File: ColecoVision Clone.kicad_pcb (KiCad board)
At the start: 2 copper layers, 149.4 x 99.1 mm, 141 parts, among them J1 Cartridge Slot, J2 Composite video, J3 PJ-102A, J4 RCJ-017, J5 Controller Port 1, J6 Controller Port 2, Q1 2n4401, Q2 Q_NJFET_DGS, Q3 2N3904, Q4 2N3904, Q5 2N3904, SW1 Power Toggle, SW2 Reset, U1 Z80CPU, U10 SN76489AN, U12 74LS138 (Mem. Mapped), U13 74LS138 (I/O), U14 74LS02, U15 Controller 1, U16 Controller 2, U17 74LS05, U18 74LS05, U19 74HC04, U2 Work RAM, U20 74LS74, U21 74HC04, U22 74LS74, U23 74HCT00, U24 TPS60403DBVR, U3 BIOS ROM 27C256, U4 74HCT04, U5 TMS9918A, U6 74LS574, U7 74LS574, U8 74LS574, U9 VRAM, X1 14.31818MHz

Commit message: TMS passive
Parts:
- moved C6 108.3 mm to (8.89, 85.7), turned to 90 degrees
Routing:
- net GND: track 841.0 -> 847.8 mm
- net VCC: track 776.2 -> 779.3 mm
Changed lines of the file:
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@@
     (thickness 1.6)
     (drawings 17)
-    (tracks 4420)
+    (tracks 4426)
     (zones 0)
     (modules 141)
@@
     (tags "resistor 0805")
     (attr smd)
-    (fp_text reference R7 (at 0 -1.7 90) (layer F.SilkS)
+    (fp_text reference R7 (at 3.6665 0.0635 90) (layer F.SilkS)
       (effects (font (size 1 1) (thickness 0.15)))
     )
@@
       (effects (font (size 1 1) (thickness 0.15)) (justify mirror))
     )
-    (fp_text value 2.7µH (at 0 -1.8 270) (layer Dwgs.User)
+    (fp_text value 2.7µH (at 0 -1.8 270) (layer Dwgs.User) hide
       (effects (font (size 1 1) (thickness 0.15)))
     )
@@
     (tags "capacitor 0805")
     (attr smd)
-    (fp_text reference C31 (at 0 -1.75) (layer F.SilkS)
+    (fp_text reference C31 (at -3.7465 0.8255) (layer F.SilkS)
       (effects (font (size 1 1) (thickness 0.15)))
     )
@@
       (effects (font (size 1 1) (thickness 0.15)))
     )
-    (fp_text user %R (at 0 -1.75) (layer F.Fab)
+    (fp_text user %R (at -3.81 0.8255) (layer F.Fab)
       (effects (font (size 1 1) (thickness 0.15)))
     )
@@
   )
   (module Capacitors_SMD:C_0805_HandSoldering (layer F.Cu)
-    (at 111.978 118.992)
+    (at 8.89 85.725 90)
     (descr "Capacitor SMD 0805, hand soldering")
     (tags "capacitor 0805")
     (attr smd)
-    (fp_text reference C6 (at 0 -1.75) (layer F.SilkS)
+    (fp_text reference C6 (at 0 -1.75 90) (layer F.SilkS)
       (effects (font (size 1 1) (thickness 0.15)))
     )
-    (fp_text value 0.1µF (at 0 1.75) (layer F.Fab)
+    (fp_text value 0.1µF (at 0 1.75 90) (layer F.Fab)
       (effects (font (size 1 1) (thickness 0.15)))
     )
-    (fp_text user %R (at 0 -1.75) (layer F.Fab)
+    (fp_text user %R (at 0 -1.75 90) (layer F.Fab)
       (effects (font (size 1 1) (thickness 0.15)))
     )
@@
     (fp_line (start 2.25 0.87) (end 2.25 -0.88) (layer F.CrtYd) (width 0.05))
     (fp_line (start 2.25 0.87) (end -2.25 0.87) (layer F.CrtYd) (width 0.05))
-    (pad 1 smd rect (at -1.25 0) (size 1.5 1.25) (layers F.Cu F.Paste F.Mask)
+    (pad 1 smd rect (at -1.25 0 90) (size 1.5 1.25) (layers F.Cu F.Paste F.Mask)
       (net 19 VCC))
-    (pad 2 smd rect (at 1.25 0) (size 1.5 1.25) (layers F.Cu F.Paste F.Mask)
+    (pad 2 smd rect (at 1.25 0 90) (size 1.5 1.25) (layers F.Cu F.Paste F.Mask)
       (net 10 GND))
     (model Capacitors_SMD.3dshapes/C_0805.wrl
@@
   (segment (start 11.002 35.386) (end 11.002 34.906) (width 0.25) (layer F.Cu) (net 10))
   (segment (start 13.208 37.592) (end 11.002 35.386) (width 0.25) (layer F.Cu) (net 10))
+  (segment (start 11.792 79.248) (end 12.192 79.248) (width 0.25) (layer F.Cu) (net 10))
+  (segment (start 8.89 82.15) (end 11.792 79.248) (width 0.25) (layer F.Cu) (net 10))
+  (segment (start 8.89 84.475) (end 8.89 82.15) (width 0.25) (layer F.Cu) (net 10))
   (segment (start 7.214 92.837) (end 7.7855 92.2655) (width 0.25) (layer F.Cu) (net 19) (status 10))
   (segment (start 6.764 92.837) (end 7.214 92.837) (width 0.25) (layer F.Cu) (net 19) (status 30))
@@
   (segment (start 19.972 38.862) (end 18.972 38.862) (width 0.25) (layer F.Cu) (net 19))
   (segment (start 18.972 38.862) (end 18.346999 38.236999) (width 0.25) (layer F.Cu) (net 19))
+  (segment (start 7.7855 89.0795) (end 7.7855 89.5735) (width 0.25) (layer F.Cu) (net 19))
+  (segment (start 8.89 87.975) (end 7.7855 89.0795) (width 0.25) (layer F.Cu) (net 19))
+  (segment (start 8.89 86.975) (end 8.89 87.975) (width 0.25) (layer F.Cu) (net 19))
   (segment (start 55.668238 114.3) (end 54.186619 115.781619) (width 0.25) (layer F.Cu) (net 22))
   (segment (start 51.052271 122.937729) (end 44.196 122.937729) (width 0.25) (layer F.Cu) (net 22))

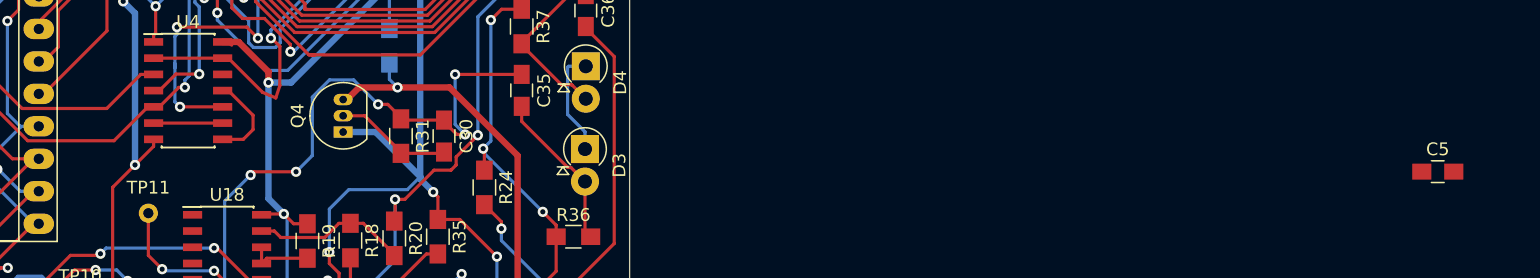
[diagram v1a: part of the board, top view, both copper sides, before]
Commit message: U4 passive
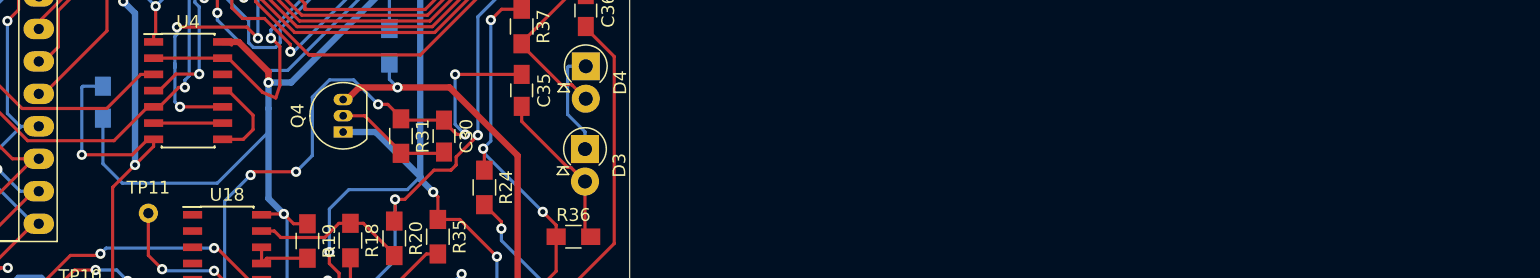
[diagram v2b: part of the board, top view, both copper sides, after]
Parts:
- C5: moved to B.Cu
- moved C5 104.6 mm to (32.4, 90.1), turned to 90 degrees
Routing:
- net VCC: track 779.3 -> 799.9 mm
- net GND: track 847.8 -> 860.9 mm, vias 47 -> 48
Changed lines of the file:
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@@
     (thickness 1.6)
     (drawings 17)
-    (tracks 4426)
+    (tracks 4439)
     (zones 0)
     (modules 141)
@@
     )
   )
-  (module Capacitors_SMD:C_0805_HandSoldering (layer F.Cu)
-    (at 136.888 95.492)
+  (module Capacitors_SMD:C_0805_HandSoldering (layer B.Cu)
+    (at 32.4485 90.063 90)
     (descr "Capacitor SMD 0805, hand soldering")
     (tags "capacitor 0805")
     (attr smd)
-    (fp_text reference C5 (at 0 -1.75) (layer F.SilkS)
-      (effects (font (size 1 1) (thickness 0.15)))
+    (fp_text reference C5 (at 0 1.75 90) (layer B.SilkS)
+      (effects (font (size 1 1) (thickness 0.15)) (justify mirror))
     )
-    (fp_text value 0.1µF (at 0 1.75) (layer F.Fab)
-      (effects (font (size 1 1) (thickness 0.15)))
+    (fp_text value 0.1µF (at 0 -1.75 90) (layer B.Fab)
+      (effects (font (size 1 1) (thickness 0.15)) (justify mirror))
     )
-    (fp_text user %R (at 0 -1.75) (layer F.Fab)
-      (effects (font (size 1 1) (thickness 0.15)))
+    (fp_text user %R (at 0 1.75 90) (layer B.Fab)
+      (effects (font (size 1 1) (thickness 0.15)) (justify mirror))
     )
-    (fp_line (start -1 0.62) (end -1 -0.62) (layer F.Fab) (width 0.1))
-    (fp_line (start 1 0.62) (end -1 0.62) (layer F.Fab) (width 0.1))
-    (fp_line (start 1 -0.62) (end 1 0.62) (layer F.Fab) (width 0.1))
-    (fp_line (start -1 -0.62) (end 1 -0.62) (layer F.Fab) (width 0.1))
-    (fp_line (start 0.5 -0.85) (end -0.5 -0.85) (layer F.SilkS) (width 0.12))
-    (fp_line (start -0.5 0.85) (end 0.5 0.85) (layer F.SilkS) (width 0.12))
-    (fp_line (start -2.25 -0.88) (end 2.25 -0.88) (layer F.CrtYd) (width 0.05))
-    (fp_line (start -2.25 -0.88) (end -2.25 0.87) (layer F.CrtYd) (width 0.05))
-    (fp_line (start 2.25 0.87) (end 2.25 -0.88) (layer F.CrtYd) (width 0.05))
-    (fp_line (start 2.25 0.87) (end -2.25 0.87) (layer F.CrtYd) (width 0.05))
-    (pad 1 smd rect (at -1.25 0) (size 1.5 1.25) (layers F.Cu F.Paste F.Mask)
+    (fp_line (start -1 -0.62) (end -1 0.62) (layer B.Fab) (width 0.1))
+    (fp_line (start 1 -0.62) (end -1 -0.62) (layer B.Fab) (width 0.1))
+    (fp_line (start 1 0.62) (end 1 -0.62) (layer B.Fab) (width 0.1))
+    (fp_line (start -1 0.62) (end 1 0.62) (layer B.Fab) (width 0.1))
+    (fp_line (start 0.5 0.85) (end -0.5 0.85) (layer B.SilkS) (width 0.12))
+    (fp_line (start -0.5 -0.85) (end 0.5 -0.85) (layer B.SilkS) (width 0.12))
+    (fp_line (start -2.25 0.88) (end 2.25 0.88) (layer B.CrtYd) (width 0.05))
+    (fp_line (start -2.25 0.88) (end -2.25 -0.87) (layer B.CrtYd) (width 0.05))
+    (fp_line (start 2.25 -0.87) (end 2.25 0.88) (layer B.CrtYd) (width 0.05))
+    (fp_line (start 2.25 -0.87) (end -2.25 -0.87) (layer B.CrtYd) (width 0.05))
+    (pad 1 smd rect (at -1.25 0 90) (size 1.5 1.25) (layers B.Cu B.Paste B.Mask)
       (net 19 VCC))
-    (pad 2 smd rect (at 1.25 0) (size 1.5 1.25) (layers F.Cu F.Paste F.Mask)
+    (pad 2 smd rect (at 1.25 0 90) (size 1.5 1.25) (layers B.Cu B.Paste B.Mask)
       (net 10 GND))
     (model Capacitors_SMD.3dshapes/C_0805.wrl
@@
   (segment (start 8.89 82.15) (end 11.792 79.248) (width 0.25) (layer F.Cu) (net 10))
   (segment (start 8.89 84.475) (end 8.89 82.15) (width 0.25) (layer F.Cu) (net 10))
+  (segment (start 35.966 92.964) (end 34.7595 94.1705) (width 0.25) (layer F.Cu) (net 10))
+  (segment (start 36.416 92.964) (end 35.966 92.964) (width 0.25) (layer F.Cu) (net 10))
+  (via (at 30.7975 94.1705) (size 0.8) (drill 0.4) (layers F.Cu B.Cu) (net 10))
+  (segment (start 34.7595 94.1705) (end 30.7975 94.1705) (width 0.25) (layer F.Cu) (net 10))
+  (segment (start 30.7975 94.1705) (end 30.7975 88.9) (width 0.25) (layer B.Cu) (net 10))
+  (segment (start 30.8845 88.813) (end 32.4485 88.813) (width 0.25) (layer B.Cu) (net 10))
+  (segment (start 30.7975 88.9) (end 30.8845 88.813) (width 0.25) (layer B.Cu) (net 10))
   (segment (start 7.214 92.837) (end 7.7855 92.2655) (width 0.25) (layer F.Cu) (net 19) (status 10))
   (segment (start 6.764 92.837) (end 7.214 92.837) (width 0.25) (layer F.Cu) (net 19) (status 30))
@@
   (via (at 45.4025 88.519) (size 0.8) (drill 0.4) (layers F.Cu B.Cu) (net 19))
   (segment (start 45.4025 97.5995) (end 46.609 98.806) (width 0.5) (layer B.Cu) (net 19))
-  (segment (start 45.4025 88.519) (end 45.4025 97.5995) (width 0.5) (layer B.Cu) (net 19))
   (segment (start 67.912 100.584) (end 67.912 103.284) (width 0.25) (layer F.Cu) (net 19) (status 10))
   (segment (start 67.912 103.284) (end 63.5 107.696) (width 0.25) (layer F.Cu) (net 19))
@@
   (segment (start 8.89 87.975) (end 7.7855 89.0795) (width 0.25) (layer F.Cu) (net 19))
   (segment (start 8.89 86.975) (end 8.89 87.975) (width 0.25) (layer F.Cu) (net 19))
+  (segment (start 32.4485 91.313) (end 32.4485 94.869) (width 0.25) (layer B.Cu) (net 19))
+  (segment (start 32.4485 94.869) (end 33.9725 96.393) (width 0.25) (layer B.Cu) (net 19))
+  (segment (start 33.9725 96.393) (end 41.402 96.393) (width 0.25) (layer B.Cu) (net 19))
+  (segment (start 41.402 96.393) (end 45.4025 92.3925) (width 0.25) (layer B.Cu) (net 19))
+  (segment (start 45.4025 92.3925) (end 45.4025 90.551) (width 0.25) (layer B.Cu) (net 19))
+  (segment (start 45.4025 90.551) (end 45.4025 97.5995) (width 0.5) (layer B.Cu) (net 19))
+  (segment (start 45.4025 88.519) (end 45.4025 90.551) (width 0.5) (layer B.Cu) (net 19))
   (segment (start 55.668238 114.3) (end 54.186619 115.781619) (width 0.25) (layer F.Cu) (net 22))
   (segment (start 51.052271 122.937729) (end 44.196 122.937729) (width 0.25) (layer F.Cu) (net 22))

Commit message: More decouplers
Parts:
- C8: moved to B.Cu
- moved C1 160.9 mm to (101.3, 86.8)
- moved C7 103.3 mm to (61.2, 46.8)
- moved C8 70.2 mm to (63.8, 70.5), turned to 270 degrees
- moved C15 23.0 mm to (227.9, 94.4)
- moved C18 12.7 mm to (239.6, 103.9)
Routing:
- net VCC: track 799.9 -> 839.4 mm, vias 42 -> 43
- net GND: track 860.9 -> 871.5 mm

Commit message: more labels
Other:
- board text added: "-5v generation"
- board text added: "a0"
- board text added: "d0"
- board text added: "long edge is pin 1"
- board text removed: "RAM_CE"
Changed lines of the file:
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@@
   (general
     (thickness 1.6)
-    (drawings 17)
+    (drawings 20)
     (tracks 4469)
     (zones 0)
@@
       (xy -3.70249 -1.164682) (xy -3.429 -1.183342) (xy -2.925182 -1.118187)) (layer F.SilkS) (width 0.01))
   )
-  (gr_text RAM_CE (at -46.0375 123.19) (layer B.SilkS)
+  (gr_text "-5v\ngeneration" (at 36.8935 105.8545) (layer B.SilkS)
+    (effects (font (size 1 1) (thickness 0.15)) (justify mirror))
+  )
+  (gr_text a0 (at -38.9255 33.4645) (layer B.SilkS)
+    (effects (font (size 1 1) (thickness 0.15)) (justify mirror))
+  )
+  (gr_text d0 (at -41.529 33.4645) (layer B.SilkS)
+    (effects (font (size 1 1) (thickness 0.15)) (justify mirror))
+  )
+  (gr_text "long edge is pin 1" (at -4.8895 69.1515) (layer B.SilkS)
     (effects (font (size 1 1) (thickness 0.15)) (justify mirror))
   )

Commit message: More labels
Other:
- board text added: "3"
- board text added: "7"
- board text added: "gnd"
- board text added: "mhz"
- board text added: "power"
- board text added: "sound"
- board text added: "video"
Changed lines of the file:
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@@
   (general
     (thickness 1.6)
-    (drawings 20)
+    (drawings 27)
     (tracks 4469)
     (zones 0)
@@
       (xy -3.70249 -1.164682) (xy -3.429 -1.183342) (xy -2.925182 -1.118187)) (layer F.SilkS) (width 0.01))
   )
+  (gr_text power (at -60.3885 33.7185) (layer F.SilkS)
+    (effects (font (size 1 1) (thickness 0.15)))
+  )
+  (gr_text gnd (at -57.3405 29.337) (layer F.SilkS)
+    (effects (font (size 1 1) (thickness 0.15)))
+  )
+  (gr_text video (at 59.055 32.7025) (layer F.SilkS)
+    (effects (font (size 1 1) (thickness 0.15)))
+  )
+  (gr_text sound (at 15.875 32.8295) (layer F.SilkS)
+    (effects (font (size 1 1) (thickness 0.15)))
+  )
+  (gr_text mhz (at -1.016 49.5935) (layer F.SilkS)
+    (effects (font (size 1 1) (thickness 0.15)))
+  )
+  (gr_text 3 (at 0.3175 50.8635) (layer F.SilkS)
+    (effects (font (size 1 1) (thickness 0.15)))
+  )
+  (gr_text 7 (at -2.286 50.8635) (layer F.SilkS)
+    (effects (font (size 1 1) (thickness 0.15)))
+  )
   (gr_text "-5v\ngeneration" (at 36.8935 105.8545) (layer B.SilkS)
